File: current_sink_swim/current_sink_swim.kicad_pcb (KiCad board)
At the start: 2 copper layers, 49.3 x 42.6 mm, 24 parts, among them J1 Conn_01x02_Socket, J2 Conn_01x03_Socket, J3 Conn_01x02_Socket, J4 Conn_01x01_Pin, Q2 IRF540N, U1 LMV358, U3 TC1016

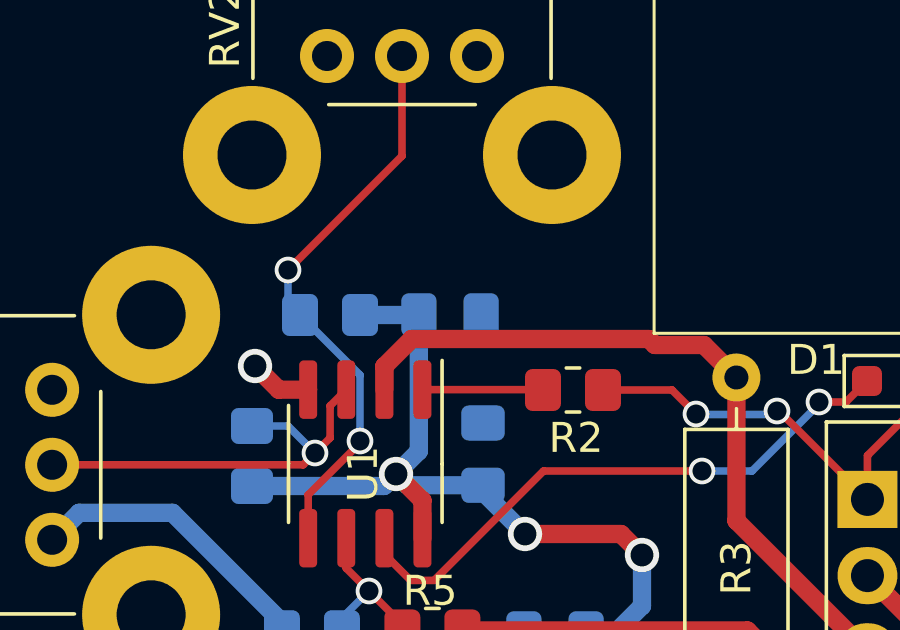
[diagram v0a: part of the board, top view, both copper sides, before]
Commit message: add part numbers and BOM
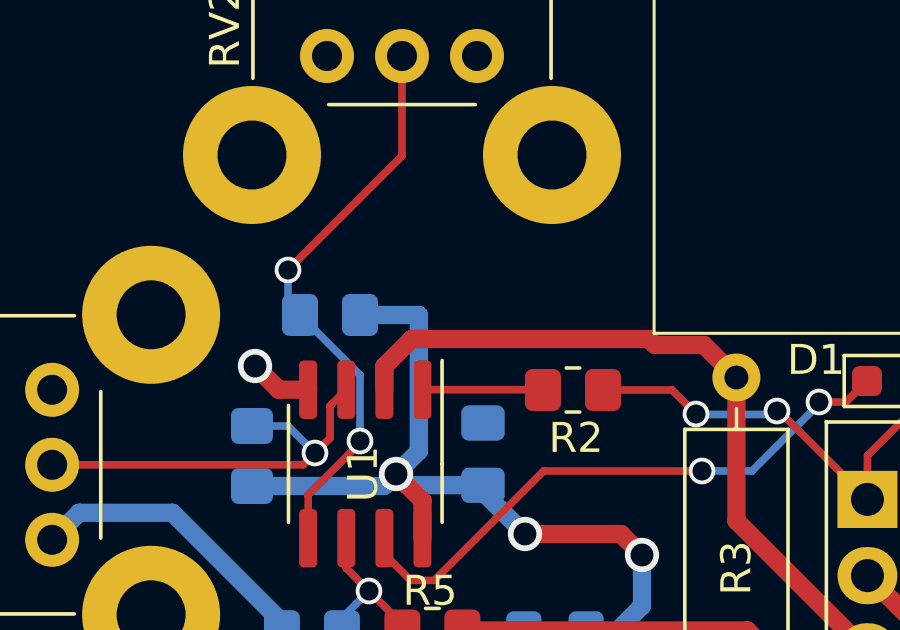
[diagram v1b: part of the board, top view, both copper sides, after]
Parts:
- removed C2: C, Capacitor_SMD:C_0805_2012Metric_Pad1.18x1.45mm_HandSolder
- R9: value 21.6k -> 21.5k
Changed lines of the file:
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@@
     (grid_origin 106.7816 71.5772)
     (pcbplotparams
-      (layerselection 0x00010fc_ffffffff)
+      (layerselection 0x00010f0_ffffffff)
       (plot_on_all_layers_selection 0x0000000_00000000)
       (disableapertmacros false)
@@
       (psa4output false)
       (plotreference true)
-      (plotvalue true)
+      (plotvalue false)
       (plotinvisibletext false)
       (sketchpadsonfab false)
-      (subtractmaskfromsilk false)
+      (subtractmaskfromsilk true)
       (outputformat 1)
       (mirror false)
-      (drillshape 1)
+      (drillshape 0)
       (scaleselection 1)
-      (outputdirectory "")
+      (outputdirectory "gerber/")
     )
   )
@@
         (effects (font (size 1 1) (thickness 0.15)))
     )
-    (fp_text value "21.6k" (at 0 1.65) (layer "F.Fab") hide
+    (fp_text value "21.5k" (at 0 1.65) (layer "F.Fab") hide
         (effects (font (size 1 1) (thickness 0.15)))
     )
@@
     (descr "Through hole angled pin header, 1x02, 2.54mm pitch, 6mm pin length, single row")
     (tags "Through hole angled pin header THT 1x02 2.54mm single row")
+    (property "MPN" "282834-2")
     (property "Sheetfile" "current_sink_swim.kicad_sch")
     (property "Sheetname" "")
@@
     (model "${KICAD6_3DMODEL_DIR}/Capacitor_SMD.3dshapes/C_0805_2012Metric.wrl"
       (offset (xyz 0 0 0))
-      (scale (xyz 1 1 1))
-      (rotate (xyz 0 0 0))
-    )
-  )
-  (footprint "Capacitor_SMD:C_0805_2012Metric_Pad1.18x1.45mm_HandSolder" (layer "B.Cu")
-    (at 123.6 41.3)
-    (descr "Capacitor SMD 0805 (2012 Metric), square (rectangular) end terminal, IPC_7351 nominal with elongated pad for handsoldering. (Body size source: IPC-SM-782 page 76, https://www.pcb-3d.com/wordpress/wp-content/uploads/ipc-sm-782a_amendment_1_and_2.pdf, https://docs.google.com/spreadsheets/d/1BsfQQcO9C6DZCsRaXUlFlo91Tg2WpOkGARC1WS5S8t0/edit?usp=sharing), generated with kicad-footprint-generator")
-    (tags "capacitor handsolder")
-    (property "Sheetfile" "voltage_control.kicad_sch")
-    (property "Sheetname" "Voltage Control")
-    (property "ki_description" "Unpolarized capacitor")
-    (property "ki_keywords" "cap capacitor")
-    (attr smd)
-    (fp_text reference "C2" (at 0 1.68) (layer "B.SilkS")
-        (effects (font (size 1 1) (thickness 0.15)) (justify mirror))
-    )
-    (fp_text value "C" (at 0 -1.68) (layer "B.Fab")
-        (effects (font (size 1 1) (thickness 0.15)) (justify mirror))
-    )
-    (fp_text user "${REFERENCE}" (at 0 0) (layer "B.Fab")
-        (effects (font (size 0.5 0.5) (thickness 0.08)) (justify mirror))
-    )
-    (fp_line (start -0.261252 -0.735) (end 0.261252 -0.735)
-      (stroke (width 0.12) (type solid)) (layer "B.SilkS"))
-    (fp_line (start -0.261252 0.735) (end 0.261252 0.735)
-      (stroke (width 0.12) (type solid)) (layer "B.SilkS"))
-    (fp_line (start -1.88 -0.98) (end -1.88 0.98)
-      (stroke (width 0.05) (type solid)) (layer "B.CrtYd"))
-    (fp_line (start -1.88 0.98) (end 1.88 0.98)
-      (stroke (width 0.05) (type solid)) (layer "B.CrtYd"))
-    (fp_line (start 1.88 -0.98) (end -1.88 -0.98)
-      (stroke (width 0.05) (type solid)) (layer "B.CrtYd"))
-    (fp_line (start 1.88 0.98) (end 1.88 -0.98)
-      (stroke (width 0.05) (type solid)) (layer "B.CrtYd"))
-    (fp_line (start -1 -0.625) (end -1 0.625)
-      (stroke (width 0.1) (type solid)) (layer "B.Fab"))
-    (fp_line (start -1 0.625) (end 1 0.625)
-      (stroke (width 0.1) (type solid)) (layer "B.Fab"))
-    (fp_line (start 1 -0.625) (end -1 -0.625)
-      (stroke (width 0.1) (type solid)) (layer "B.Fab"))
-    (fp_line (start 1 0.625) (end 1 -0.625)
-      (stroke (width 0.1) (type solid)) (layer "B.Fab"))
-    (pad "1" smd roundrect (at -1.0375 0) (size 1.175 1.45) (layers "B.Cu" "B.Paste" "B.Mask") (roundrect_rratio 0.2127659574)
-      (net 1 "2.7V") (pintype "passive"))
-    (pad "2" smd roundrect (at 1.0375 0) (size 1.175 1.45) (layers "B.Cu" "B.Paste" "B.Mask") (roundrect_rratio 0.2127659574)
-      (net 6 "Current_Sink-") (pintype "passive"))
-    (model "${KICAD6_3DMODEL_DIR}/Capacitor_SMD.3dshapes/C_0805_2012Metric.wrl"
-      (offset (xyz 0 0 0))
